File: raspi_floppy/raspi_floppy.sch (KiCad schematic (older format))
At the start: 22 parts, among them J1 Raspberry_Pi_2_3, J5 Conn_02x17_Odd_Even, U1 74LS06, U2 74LS06

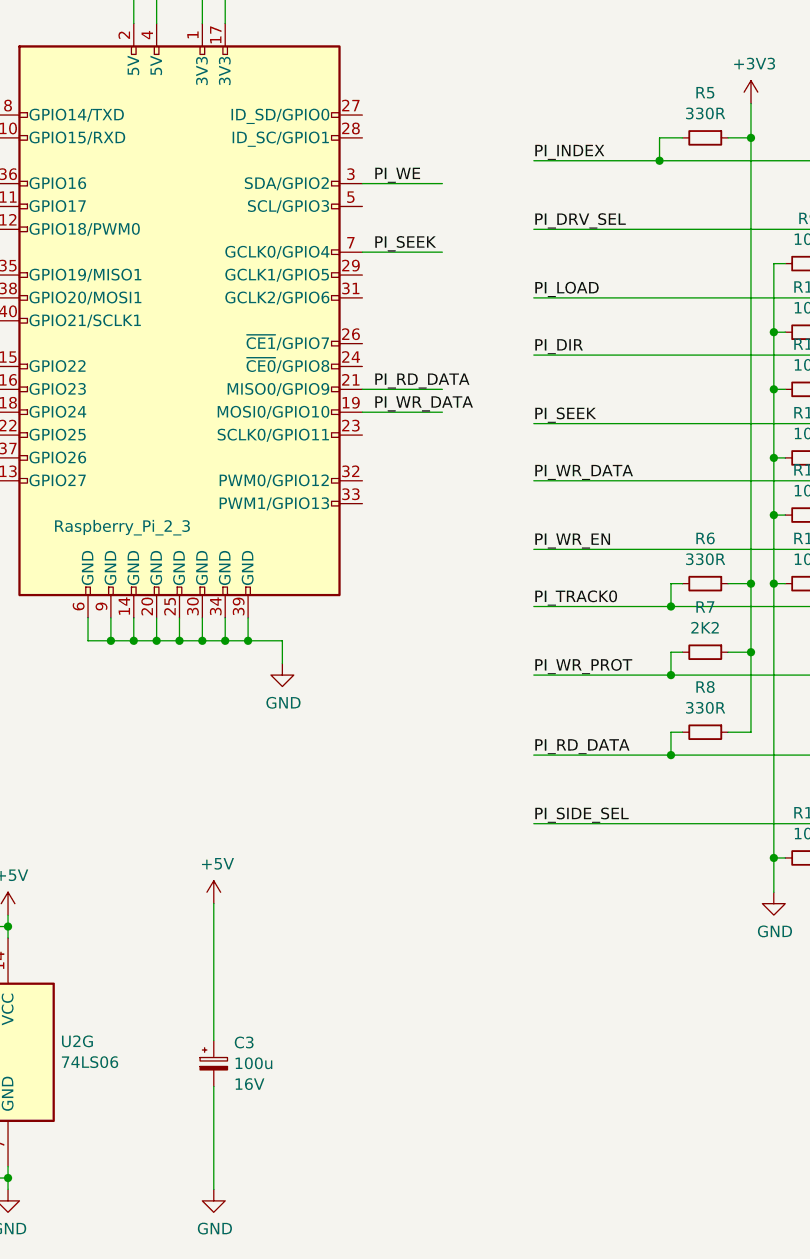
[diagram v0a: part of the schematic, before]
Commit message: Update Pi floppy i/f.
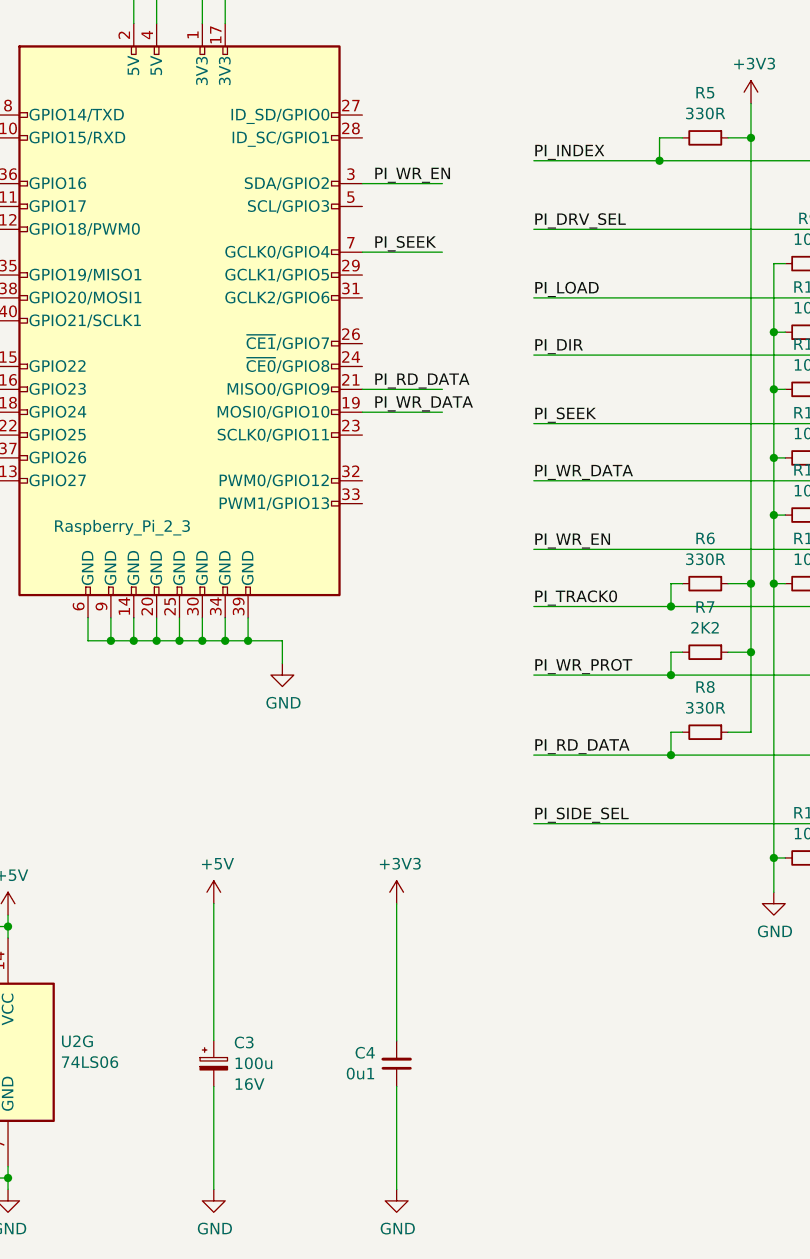
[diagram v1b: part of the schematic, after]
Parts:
- added C4: 0u1, Capacitors_ThroughHole:C_Disc_D3.4mm_W2.1mm_P2.50mm, symbol Device:C_Small
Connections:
- net labels removed: PI_WE
- wire segments 204 -> 206
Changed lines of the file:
@@
 	3750 2450 4100 2450
 Text Label 3800 2450 0    50   ~ 0
-PI_WE
+PI_WR_EN
 Wire Wire Line
 	3750 2750 4100 2750
@@
 	0    1    1    0
 $EndComp
+$Comp
+L Device:C_Small C4
+U 1 1 6009941D
+P 3900 6300
+F 0 "C4" H 3808 6254 50  0000 R CNN
+F 1 "0u1" H 3808 6345 50  0000 R CNN
+F 2 "Capacitors_ThroughHole:C_Disc_D3.4mm_W2.1mm_P2.50mm" H 3900 6300 50  0001 C CNN
+F 3 "~" H 3900 6300 50  0001 C CNN
+	1    3900 6300
+	1    0    0    1
+$EndComp
+$Comp
+L power:GND #PWR016
+U 1 1 600A5F2C
+P 3900 6850
+F 0 "#PWR016" H 3900 6600 50  0001 C CNN
+F 1 "GND" H 3905 6677 50  0000 C CNN
+F 2 "" H 3900 6850 50  0001 C CNN
+F 3 "" H 3900 6850 50  0001 C CNN
+	1    3900 6850
+	1    0    0    -1
+$EndComp
+Wire Wire Line
+	3900 6850 3900 6400
+$Comp
+L power:+3V3 #PWR015
+U 1 1 600C02BF
+P 3900 5600
+F 0 "#PWR015" H 3900 5450 50  0001 C CNN
+F 1 "+3V3" H 3915 5773 50  0000 C CNN
+F 2 "" H 3900 5600 50  0001 C CNN
+F 3 "" H 3900 5600 50  0001 C CNN
+	1    3900 5600
+	1    0    0    -1
+$EndComp
+Wire Wire Line
+	3900 5600 3900 6200
 $EndSCHEMATC
